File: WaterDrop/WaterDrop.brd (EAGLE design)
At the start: 20 x 35 mm, 12 parts, among them IC1 PIC12F1822

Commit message: random cotroller added
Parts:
- added D1: SD0, WaterDrop:SOD-323
- added X1, X2: P-PAD-S, OSSI:P-PAD-S
- moved JP3 0.64 mm to (0.00, 0.64)
- moved C3 0.45 mm to (-2.86, 15.6)
- moved R2 0.45 mm to (2.86, 15.6)
- moved C4 0.32 mm to (2.86, 14.0)
- moved R1 0.32 mm to (-2.86, 14.0)
- moved C2 0.32 mm to (0.00, 15.6)
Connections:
- net +5V: now also D1.1
- net GND: now also D1.2, X2.1
- net PIEZO: now also X1.1
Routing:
- net GND: track 0.00 -> 54.9 mm, vias 0 -> 3
- net +5V: track 0.00 -> 21.0 mm, vias 0 -> 1
- net /RST: track 0.00 -> 16.5 mm
- net PIEZO: track 0.00 -> 15.5 mm, vias 0 -> 1
- net ICSPDAT: track 0.00 -> 11.8 mm
- net ICSPCLK: track 0.00 -> 7.72 mm
- net N$3: track 0.00 -> 4.73 mm
- net N$2: track 0.00 -> 1.04 mm
- added copper zone on layer 16, net N$1
- added copper zone on layer 1, net STRUT_GND
- added copper zone on layer 16, net STRUT_GND
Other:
- outline, holes or cut-outs redrawn
- board text removed: "5V TVS diode"
- board text removed: "Chassis GND Guard Ring"
- board text removed: "How To Fix the Cable?"
- board text removed: "SMD pads for piezo spkr"

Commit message: waterdrop and random controller gerber
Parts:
- removed X1, X2: P-PAD-S, OSSI:P-PAD-S
- added U$1: LOGOPIEZO, WaterDrop:SSPIEZOLOGO
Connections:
- net GND: no longer X2.1
- net PIEZO: no longer X1.1
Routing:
- net GND: track 54.9 -> 53.0 mm
- net PIEZO: track 15.5 -> 14.2 mm
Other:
- board size 20 x 35 mm -> 20 x 40 mm

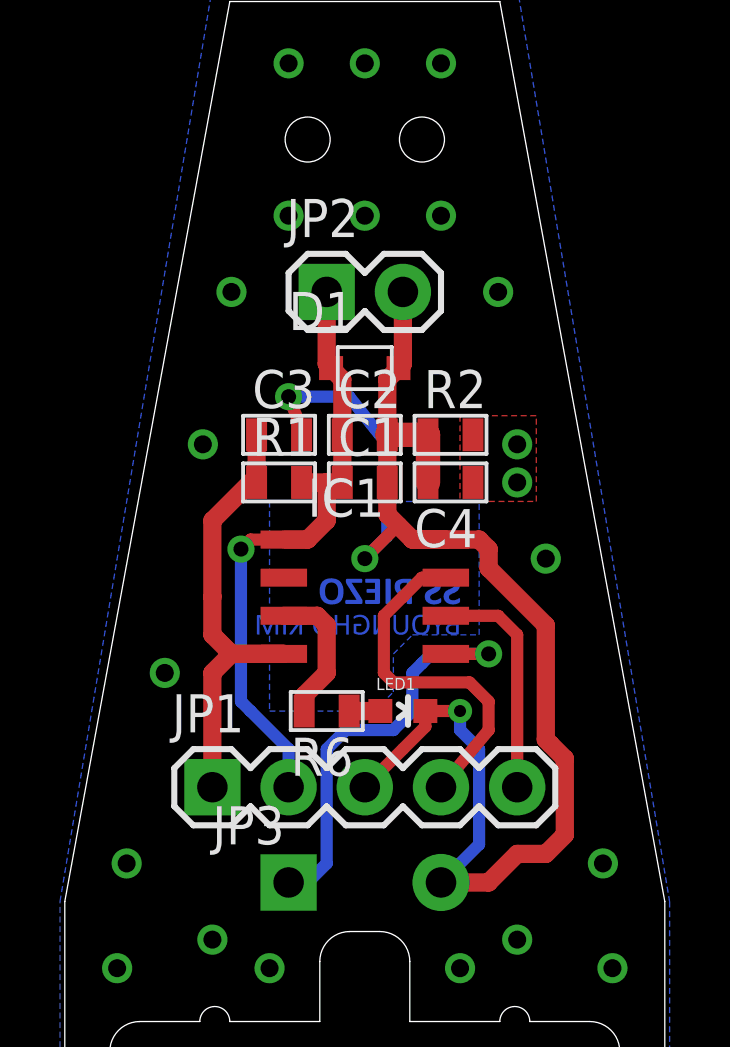
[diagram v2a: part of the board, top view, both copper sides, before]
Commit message: schmatic renumbered final merged gerber for fab
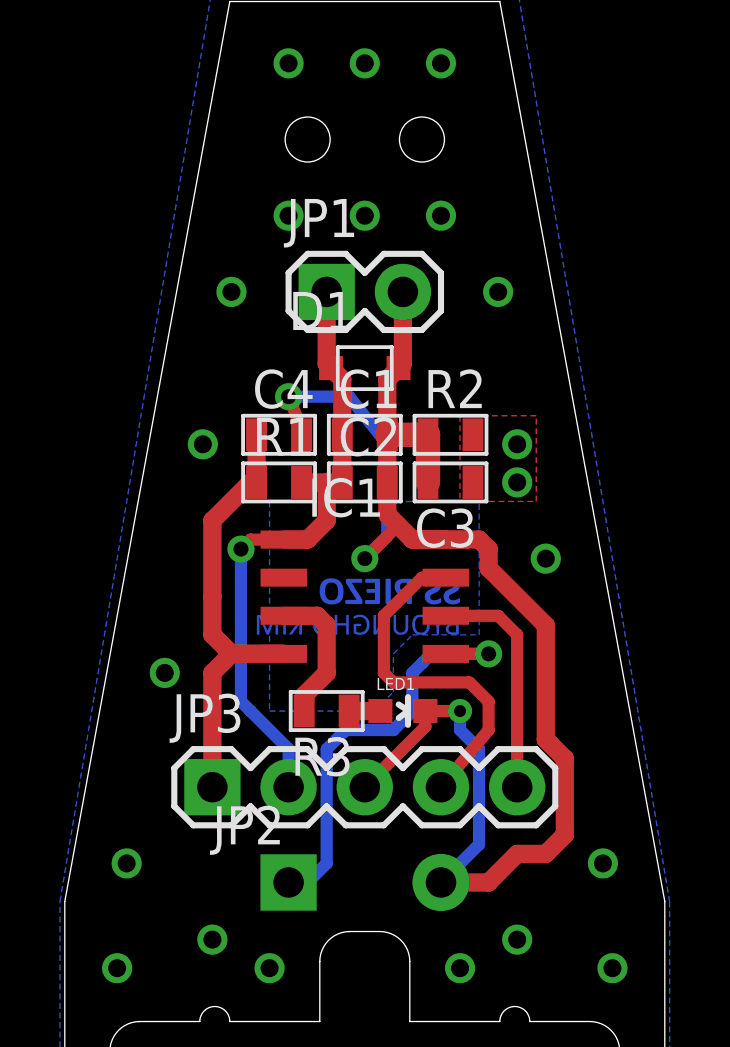
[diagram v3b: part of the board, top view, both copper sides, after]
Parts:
- C1: value 0.1uF -> 100pF
- C2: value 100pF -> 0.1uF
- JP1: value (none) -> M02PTH; device SparkFun-Connectors:1X05 -> SparkFun-Connectors:1X02
- JP2: value M02PTH -> 2PIN; device SparkFun-Connectors:1X02 -> WaterDrop:2PIN5.08
- JP3: value 2PIN -> (none); device WaterDrop:2PIN5.08 -> SparkFun-Connectors:1X05
- moved JP2 19.7 mm to (0.00, 0.64)
- moved JP1 16.9 mm to (-1.27, 20.3)
- moved JP3 5.99 mm to (-5.08, 3.81)
- moved C3 5.93 mm to (2.86, 14.0), turned to 180 degrees
- moved C4 5.93 mm to (-2.86, 15.6), turned to 0 degrees
- moved C1 1.59 mm to (0.00, 15.6)
- moved C2 1.59 mm to (0.00, 14.0)
- renumbered R6 to R3
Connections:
- net +5V: now also JP1.1, JP3.2; no longer JP1.2, JP2.1
- net /RST: now also C4.1, JP3.1; no longer C3.1, JP1.1
- net GND: now also JP1.2, JP3.3; no longer JP1.3, JP3.2
- net ICSPCLK: now also JP3.5; no longer JP1.5
- net ICSPDAT: now also JP3.4; no longer JP1.4
- net PIEZO: now also JP2.1; no longer JP3.1
- net STRUT_GND: now also C3.1; no longer C4.1
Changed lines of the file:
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@@
 <elements>
 <element name="IC1" library="WaterDrop" package="SO8" value="PIC12F1822" x="0" y="10.16" rot="R270"/>
-<element name="C1" library="WaterDrop" package="C0603(1608)" value="0.1uF" x="0" y="13.97"/>
-<element name="C2" library="WaterDrop" package="C0603(1608)" value="100pF" x="0" y="15.5575"/>
+<element name="C2" library="WaterDrop" package="C0603(1608)" value="0.1uF" x="0" y="13.97"/>
+<element name="C1" library="WaterDrop" package="C0603(1608)" value="100pF" x="0" y="15.5575"/>
 <element name="R1" library="WaterDrop" package="R0603(1608)" value="10k" x="-2.8575" y="13.97"/>
-<element name="C3" library="WaterDrop" package="C0603(1608)" value="0.1uF" x="-2.8575" y="15.5575"/>
+<element name="C4" library="WaterDrop" package="C0603(1608)" value="0.1uF" x="-2.8575" y="15.5575"/>
 <element name="R2" library="WaterDrop" package="R0603(1608)" value="1M" x="2.8575" y="15.5575"/>
-<element name="C4" library="WaterDrop" package="C0603(1608)" value="0.1uF" x="2.8575" y="13.97" rot="R180"/>
+<element name="C3" library="WaterDrop" package="C0603(1608)" value="0.1uF" x="2.8575" y="13.97" rot="R180"/>
 <element name="LED1" library="SparkFun" package="LED-0603" value="" x="1.27" y="6.35" rot="R270"/>
-<element name="R6" library="WaterDrop" package="R0603(1608)" value="2.2k" x="-1.27" y="6.35" rot="R180"/>
-<element name="JP1" library="SparkFun-Connectors" package="1X05" value="" x="-5.08" y="3.81"/>
-<element name="JP2" library="SparkFun-Connectors" package="1X02" value="M02PTH" x="-1.27" y="20.32"/>
-<element name="JP3" library="WaterDrop" package="2PIN5.08" value="2PIN" x="0" y="0.635"/>
+<element name="R3" library="WaterDrop" package="R0603(1608)" value="2.2k" x="-1.27" y="6.35" rot="R180"/>
+<element name="JP3" library="SparkFun-Connectors" package="1X05" value="" x="-5.08" y="3.81"/>
+<element name="JP1" library="SparkFun-Connectors" package="1X02" value="M02PTH" x="-1.27" y="20.32"/>
+<element name="JP2" library="WaterDrop" package="2PIN5.08" value="2PIN" x="0" y="0.635"/>
 <element name="D1" library="WaterDrop" package="SOD-323" value="SD0" x="0" y="17.78"/>
 <element name="U$1" library="WaterDrop" package="SSPIEZOLOGO" value="LOGOPIEZO" x="3.175" y="8.89" rot="MR0"/>
@@
 <signal name="+5V">
 <contactref element="IC1" pad="1"/>
+<contactref element="C2" pad="1"/>
 <contactref element="C1" pad="1"/>
-<contactref element="C2" pad="1"/>
 <contactref element="R1" pad="2"/>
-<contactref element="JP1" pad="2"/>
-<contactref element="JP2" pad="1"/>
+<contactref element="JP3" pad="2"/>
+<contactref element="JP1" pad="1"/>
 <contactref element="D1" pad="1"/>
 <wire x1="-2.1075" y1="13.97" x2="-1.27" y2="13.97" width="0.6096" layer="1"/>
@@
 <signal name="GND">
 <contactref element="IC1" pad="8"/>
+<contactref element="C2" pad="2"/>
 <contactref element="C1" pad="2"/>
-<contactref element="C2" pad="2"/>
+<contactref element="C4" pad="2"/>
+<contactref element="R2" pad="1"/>
 <contactref element="C3" pad="2"/>
-<contactref element="R2" pad="1"/>
-<contactref element="C4" pad="2"/>
 <contactref element="LED1" pad="C"/>
-<contactref element="JP1" pad="3"/>
+<contactref element="JP3" pad="3"/>
+<contactref element="JP1" pad="2"/>
 <contactref element="JP2" pad="2"/>
-<contactref element="JP3" pad="2"/>
 <contactref element="D1" pad="2"/>
 <wire x1="1.27" y1="20.32" x2="1.27" y2="17.925" width="0.6096" layer="1"/>
@@
 <signal name="PIEZO">
 <contactref element="IC1" pad="5"/>
-<contactref element="JP3" pad="1"/>
+<contactref element="JP2" pad="1"/>
 <wire x1="-2.54" y1="0.635" x2="-1.905" y2="0.635" width="0.4064" layer="16"/>
 <wire x1="-1.905" y1="0.635" x2="-1.27" y2="1.27" width="0.4064" layer="16"/>
@@
 <contactref element="IC1" pad="4"/>
 <contactref element="R1" pad="1"/>
-<contactref element="C3" pad="1"/>
-<contactref element="JP1" pad="1"/>
+<contactref element="C4" pad="1"/>
+<contactref element="JP3" pad="1"/>
 <wire x1="-3.6075" y1="15.5575" x2="-3.6075" y2="13.97" width="0.6096" layer="1"/>
 <wire x1="-2.7" y1="8.255" x2="-4.445" y2="8.255" width="0.6096" layer="1"/>
@@
 <signal name="ICSPDAT">
 <contactref element="IC1" pad="7"/>
-<contactref element="JP1" pad="4"/>
+<contactref element="JP3" pad="4"/>
 <wire x1="2.7" y1="10.795" x2="1.905" y2="10.795" width="0.4064" layer="1"/>
 <wire x1="1.905" y1="10.795" x2="1.27" y2="10.16" width="0.4064" layer="1"/>
@@
 <signal name="ICSPCLK">
 <contactref element="IC1" pad="6"/>
-<contactref element="JP1" pad="5"/>
+<contactref element="JP3" pad="5"/>
 <wire x1="2.7" y1="9.525" x2="4.445" y2="9.525" width="0.4064" layer="1"/>
 <wire x1="4.445" y1="9.525" x2="5.08" y2="8.89" width="0.4064" layer="1"/>
@@
 <signal name="N$3">
 <contactref element="IC1" pad="3"/>
-<contactref element="R6" pad="2"/>
+<contactref element="R3" pad="2"/>
 <wire x1="-2.7" y1="9.525" x2="-1.5875" y2="9.525" width="0.6096" layer="1"/>
 <wire x1="-1.5875" y1="9.525" x2="-1.27" y2="9.2075" width="0.6096" layer="1"/>
@@
 <signal name="STRUT_GND">
 <contactref element="R2" pad="2"/>
-<contactref element="C4" pad="1"/>
+<contactref element="C3" pad="1"/>
 <polygon width="0.254" layer="16" isolate="0.4064">
 <vertex x="-5.08" y="30.48"/>
@@
 <signal name="N$2">
 <contactref element="LED1" pad="A"/>
-<contactref element="R6" pad="1"/>
+<contactref element="R3" pad="1"/>
 <wire x1="0.52" y1="6.35" x2="-0.52" y2="6.35" width="0.6096" layer="1"/>
 </signal>
